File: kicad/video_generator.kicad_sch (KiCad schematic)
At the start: 37 parts, among them J1 Conn_01x10, J10 DE9_RGBI_Video, Q2 2N2219, U47 74LS393, U77 74LS95, U78 74LS95, U80 74LS157, U81 74LS95, U82 74LS95, U83 74LS95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

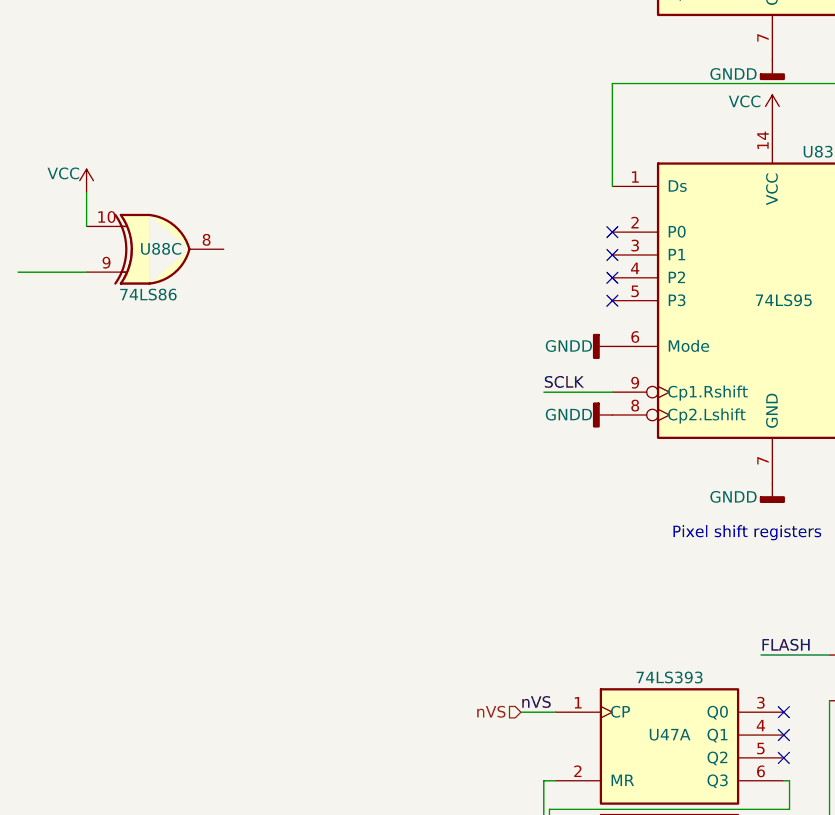
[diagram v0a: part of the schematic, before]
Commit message: add doc folder, ro and en readme
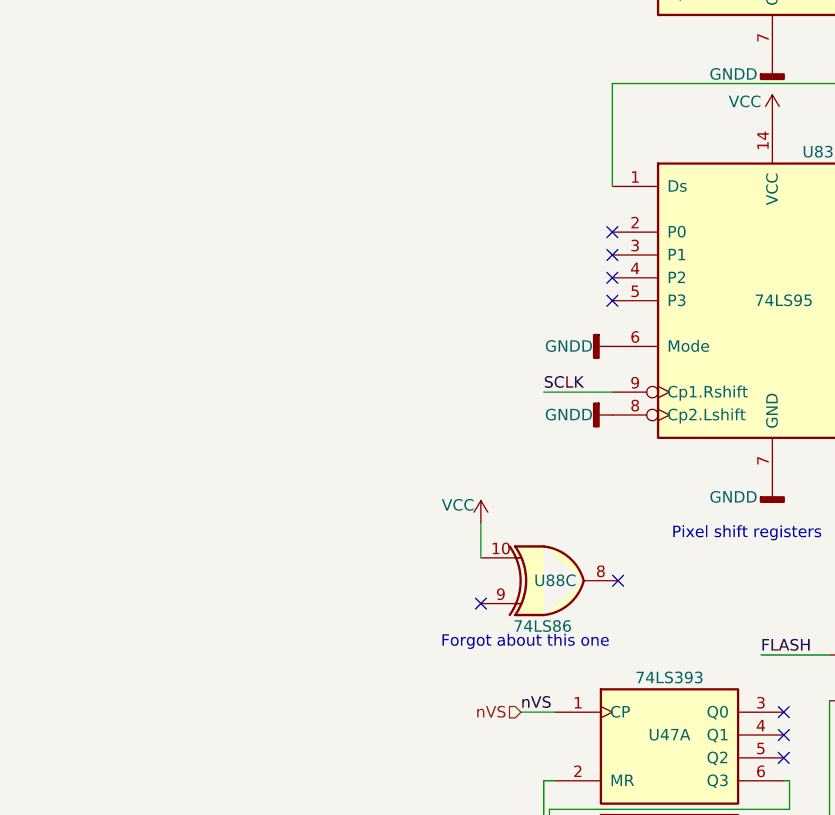
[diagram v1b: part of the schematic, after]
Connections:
- no-connect marks 20 -> 22
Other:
- note added: "Forgot about this one"
- moved on the sheet: U88C
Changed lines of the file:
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@@
   (no_connect (at 52.07 203.2))
   (no_connect (at 68.58 31.75))
+  (no_connect (at 18.415 169.545))
   (no_connect (at 68.58 29.21))
   (no_connect (at 68.58 76.2))
@@
   (no_connect (at 52.07 184.15))
   (no_connect (at 33.02 128.27))
+  (no_connect (at 33.655 167.005))
   (no_connect (at 52.07 200.66))
   (no_connect (at 52.07 198.12))
@@
     (stroke (width 0) (type default))
   )
-  (wire (pts (xy -25.4 123.825) (xy -25.4 127.635))
+  (wire (pts (xy 18.415 160.655) (xy 18.415 164.465))
     (stroke (width 0) (type default))
   )
@@
     (stroke (width 0) (type default))
   )
-  (wire (pts (xy -25.4 132.715) (xy -33.02 132.715))
-    (stroke (width 0) (type default))
-  )
   (wire (pts (xy 77.47 224.79) (xy 59.69 224.79))
     (stroke (width 0) (type default))
@@
   )
   (text "Video Attributes registers" (at 94.996 122.174 0)
+    (effects (font (size 1.27 1.27)) (justify left bottom))
+  )
+  (text "Forgot about this one" (at 13.97 174.625 0)
     (effects (font (size 1.27 1.27)) (justify left bottom))
   )
@@
     )
   )
-  (symbol (lib_id "74xx:74LS86") (at -17.78 130.175 0) (mirror x) (unit 3)
-    (in_bom yes) (on_board yes) (dnp no)
-    (property "Reference" "U88" (at -17.145 130.175 0)
-      (effects (font (size 1.27 1.27)))
-    )
-    (property "Value" "74LS86" (at -18.542 135.255 0)
-      (effects (font (size 1.27 1.27)))
-    )
-    (property "Footprint" "Cobra_original:DIP-14_W7.62mm" (at -17.78 130.175 0)
-      (effects (font (size 1.27 1.27)) hide)
-    )
-    (property "Datasheet" "74xx/74ls86.pdf" (at -17.78 130.175 0)
+  (symbol (lib_id "74xx:74LS86") (at 26.035 167.005 0) (mirror x) (unit 3)
+    (in_bom yes) (on_board yes) (dnp no)
+    (property "Reference" "U88" (at 26.67 167.005 0)
+      (effects (font (size 1.27 1.27)))
+    )
+    (property "Value" "74LS86" (at 25.273 172.085 0)
+      (effects (font (size 1.27 1.27)))
+    )
+    (property "Footprint" "Cobra_original:DIP-14_W7.62mm" (at 26.035 167.005 0)
+      (effects (font (size 1.27 1.27)) hide)
+    )
+    (property "Datasheet" "74xx/74ls86.pdf" (at 26.035 167.005 0)
       (effects (font (size 1.27 1.27)) hide)
     )
@@
     )
   )
-  (symbol (lib_id "power:VCC") (at -25.4 123.825 0) (unit 1)
-    (in_bom yes) (on_board yes) (dnp no)
-    (property "Reference" "#PWR0376" (at -25.4 127.635 0)
-      (effects (font (size 1.27 1.27)) hide)
-    )
-    (property "Value" "VCC" (at -27.94 121.793 0)
-      (effects (font (size 1.27 1.27)))
-    )
-    (property "Footprint" "" (at -25.4 123.825 0)
-      (effects (font (size 1.27 1.27)) hide)
-    )
-    (property "Datasheet" "" (at -25.4 123.825 0)
-      (effects (font (size 1.27 1.27)) hide)
-    )
+  (symbol (lib_id "power:VCC") (at 18.415 160.655 0) (unit 1)
+    (in_bom yes) (on_board yes) (dnp no)
+    (property "Reference" "#PWR0376" (at 18.415 164.465 0)
+      (effects (font (size 1.27 1.27)) hide)
+    )
+    (property "Value" "VCC" (at 15.875 158.623 0)
+      (effects (font (size 1.27 1.27)))
+    )
+    (property "Footprint" "" (at 18.415 160.655 0)
+      (effects (font (size 1.27 1.27)) hide)
+    )
+    (property "Datasheet" "" (at 18.415 160.655 0)
+      (effects (font (size 1.27 1.27)) hide)
+    )
